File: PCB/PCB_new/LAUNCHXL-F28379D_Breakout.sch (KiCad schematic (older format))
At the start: 23 parts, among them IC1 LM358N, Q1 220mA/50V/3.5Ω, Q2 100V/17A, Q3 100V/17A, Q4 100V/17A, Q5 100V/17A, Q6 100V/17A

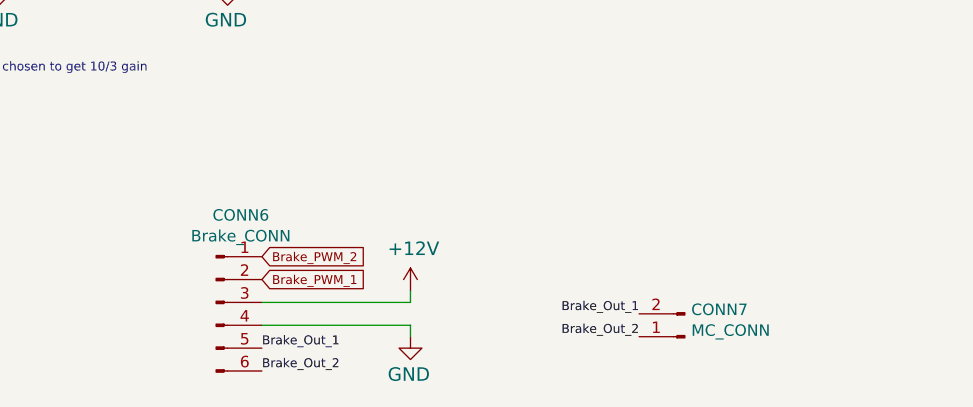
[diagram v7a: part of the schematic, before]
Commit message: fixed connector notation error
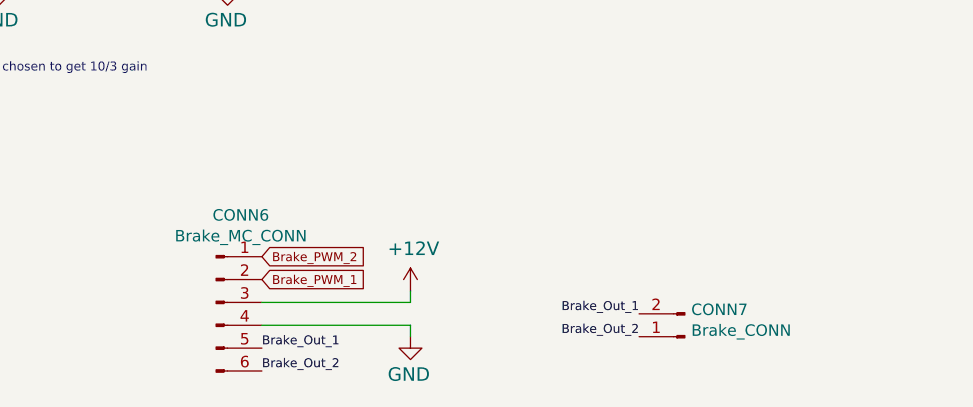
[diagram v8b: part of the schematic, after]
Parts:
- CONN6: value Brake_CONN -> Brake_MC_CONN
- CONN7: value MC_CONN -> Brake_CONN
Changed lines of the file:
@@
 P 5250 6100
 F 0 "CONN6" H 5358 6481 50  0000 C CNN
-F 1 "Brake_CONN" H 5358 6390 50  0000 C CNN
+F 1 "Brake_MC_CONN" H 5358 6390 50  0000 C CNN
 F 2 "Drivetrain_control:Brake_MC_Conn" H 5250 6100 50  0001 C CNN
 F 3 "https://cdn-shop.adafruit.com/product-files/3190/drv8871.pdf" H 5250 6100 50  0001 C CNN
@@
 P 7300 6250
 F 0 "CONN7" H 7272 6132 50  0000 R CNN
-F 1 "MC_CONN" H 7272 6223 50  0000 R CNN
+F 1 "Brake_CONN" H 7272 6223 50  0000 R CNN
 F 2 "Connector_Molex:Molex_KK-254_AE-6410-02A_1x02_P2.54mm_Vertical" H 7300 6250 50  0001 C CNN
 F 3 "~" H 7300 6250 50  0001 C CNN
